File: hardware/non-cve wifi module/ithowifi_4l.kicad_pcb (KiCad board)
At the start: 4 copper layers, 63.1 x 49.8 mm, 47 parts, among them J1 USB_B_Micro, J2 RJ45_LED_Shielded, J3 Conn_Coaxial, J4 Conn_02x02_Odd_Even, J5 Conn_02x02_Odd_Even, J6 Conn_01x02_Male, Q1 BSS138, Q2 BSS138, Q3 BC847, Q4 BC847, SW1 Fail safe, U1 ESP32-WROOM, U2 CC1101-868MHz-Module, U3 CH340G, U4 AMS1117-3.3, Y1 Crystal_GND24_Small

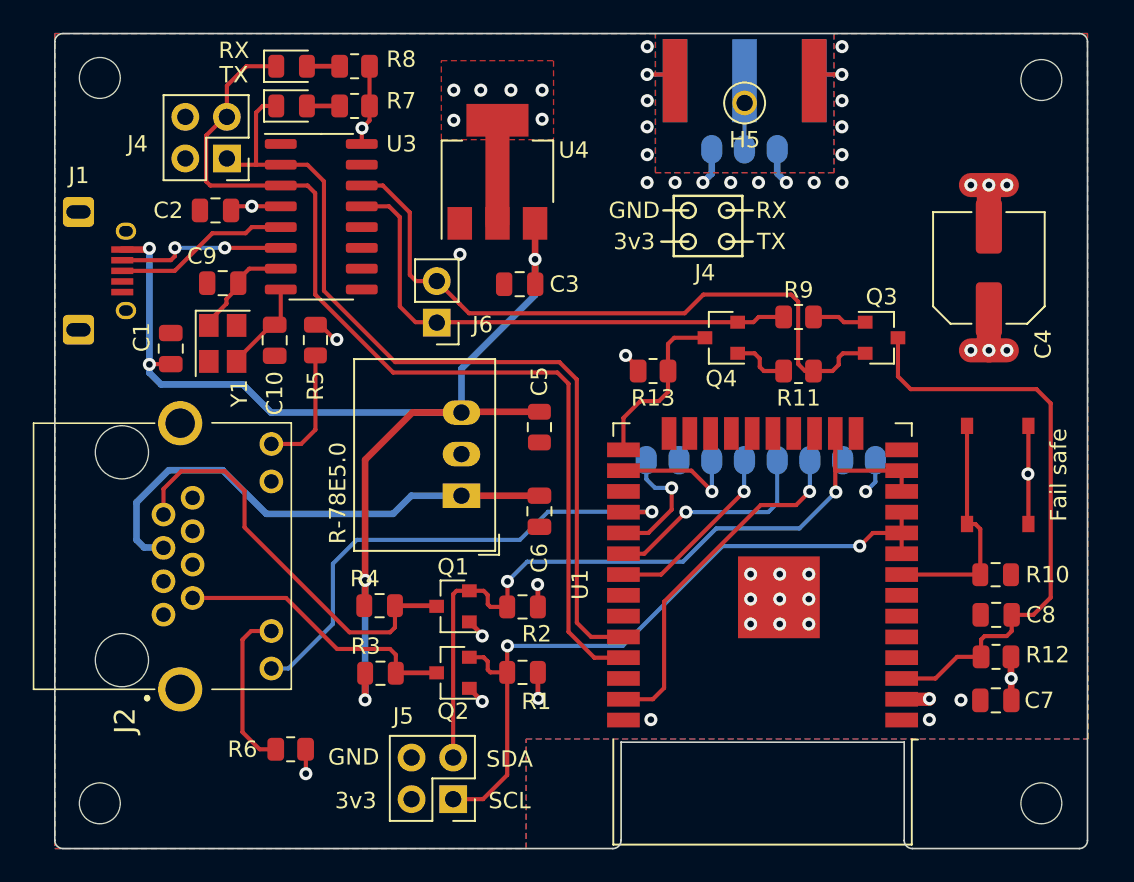
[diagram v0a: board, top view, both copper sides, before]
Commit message: Version 2.3-beta5
- fix: prevent crashes unsupported or partly supported itho devices
- breaking: On the up-side; all settings and labels have been regenerated and checked (and some translated) with a script, units have been added where available and labels are more descriptive. On the flip-side; automations based on the API, specifically the itho status label based automations might need to be updated.
- add: support for itho HeatPumt (WPU) devices and AutoTemp devices.

Please check labels for status and settings, if you see anything wrong, please let me know.
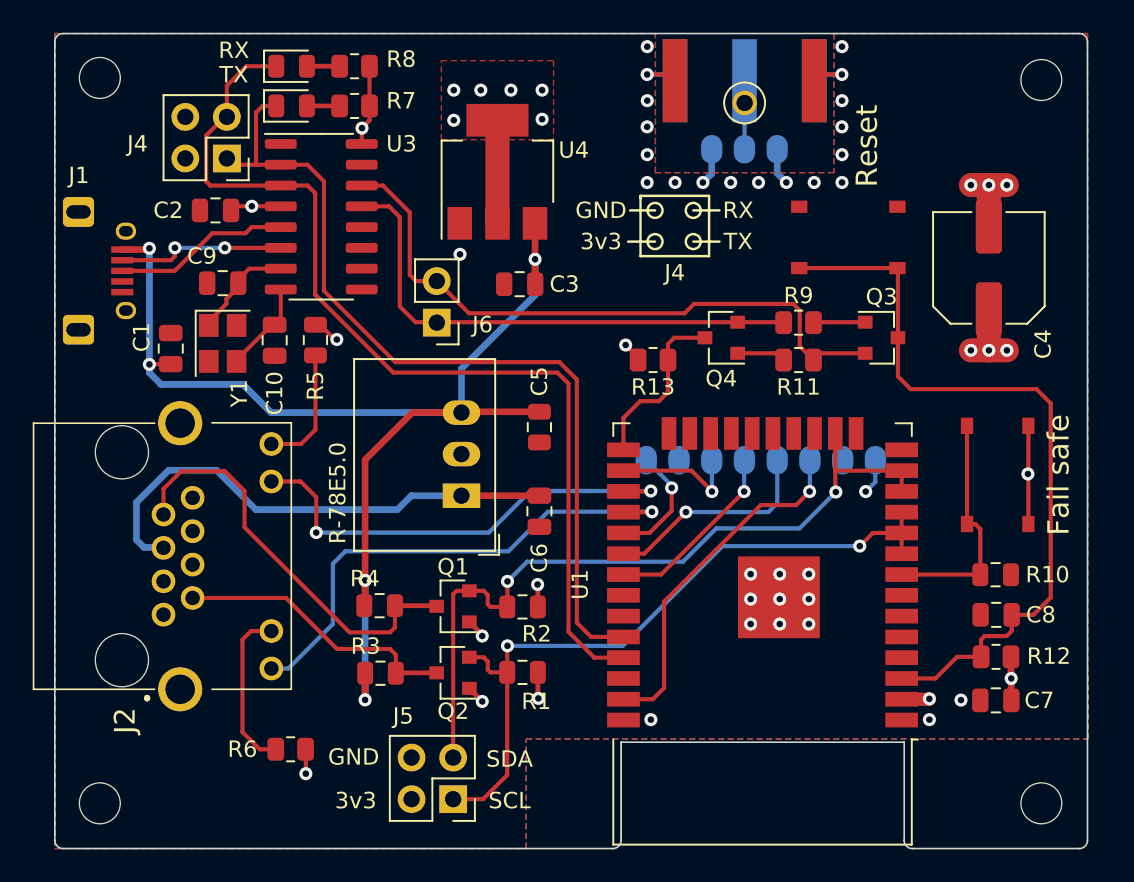
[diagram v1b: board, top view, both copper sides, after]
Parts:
- added Reset: Reset, nrg_watch:TS-1187, F.Cu at (101.2, 119.1)
- moved R11 0.67 mm to (98.2, 126.6)
- moved R13 0.67 mm to (89.3, 126.6)
- moved R9 0.35 mm to (98.2, 124.3)
- turned R12 to 0 degrees
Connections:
- J2 pad 11: GND -> D16_SYS_STATUS
- R12 pad 1: +3V3 -> EN
- R12 pad 2: EN -> +3V3
- U1 pad 27: Net-(U1-Pad27) -> D16_SYS_STATUS
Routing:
- net D16_SYS_STATUS: track 0.00 -> 32.3 mm, vias 0 -> 2
- net EN: track 36.6 -> 46.9 mm
- net RTS: track 41.6 -> 39.3 mm
- net Net-(Q4-Pad1): track 3.56 -> 2.98 mm
- net D5_SS: track 7.81 -> 7.25 mm
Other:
- board text added: "Itho HRU ESP WiFi Controller v1.2 Arjen Hiemstra - GNU GPL 3.0"
- board text removed: "Itho HRU ESP WiFi Controller v1.1 Arjen Hiemstra - GNU GPL 3.0"

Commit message: Version 2.3.5
Version 2.3.5

- fix: typo in WebAPI causing timer always being set to speed amount of minutes
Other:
- board text added: "Itho HRU ESP WiFi Controller v1.3 Arjen Hiemstra - GNU GPL 3.0"
- board text added: "https://github.com/arjenhiemstra/ithowifi"
- board text removed: "Itho HRU ESP WiFi Controller v1.2 Arjen Hiemstra - GNU GPL 3.0"
- board text removed: "https://github.com/arjenhiemstra/ithohruwifi"

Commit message: Update HW files and correct spelling
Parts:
- removed J6: Conn_01x02_Male, Connector_PinHeader_2.54mm:PinHeader_1x02_P2.54mm_Vertical
- moved C4 18.8 mm to (91.0, 120.8), turned to 0 degrees
- moved R13 11.2 mm to (100.5, 127.1), turned to 90 degrees
- moved Q4 10.6 mm to (103.9, 127.3), turned to 270 degrees
- moved SW2 9.83 mm to (110.4, 122.7), turned to 270 degrees
- moved R11 7.84 mm to (105.3, 123.3), turned to 270 degrees
- moved Q3 5.89 mm to (103.8, 119.4), turned to 90 degrees
- moved R9 4.93 mm to (103.0, 123.3), turned to 90 degrees
- renumbered Reset to SW2
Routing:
- net EN: track 46.9 -> 24.2 mm
- net DTR: track 31.9 -> 9.42 mm
- net RTS: track 39.3 -> 26.1 mm
- net +5V: track 75.6 -> 63.3 mm, vias 5 -> 4
- net D0: track 10.7 -> 0.00 mm
- net Net-(Q3-Pad1): track 3.17 -> 0.00 mm
- net Net-(Q4-Pad1): track 2.98 -> 0.00 mm
- net GND: track 16.7 -> 16.3 mm, vias 34 -> 33

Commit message: Update hardware design files
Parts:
- removed J3: Conn_Coaxial, Connector_Coaxial:SMA_Amphenol_132289_EdgeMount
- Q1, Q2, Q3, Q4: footprint Package_TO_SOT_SMD:SOT-23 -> Package_TO_SOT_SMD:SOT-23W
- U1: footprint RF_Module:ESP32-WROOM-32 -> nrg_watch:ESP32-WROOM-32E
- moved C4 11.3 mm to (79.9, 122.6)
- moved R13 11.2 mm to (89.3, 127.9), turned to 180 degrees
- moved Q4 10.5 mm to (93.5, 126.5), turned to 180 degrees
- moved R11 8.43 mm to (98.2, 127.9), turned to 180 degrees
- moved Q3 7.12 mm to (103.2, 126.5), turned to 0 degrees
- moved C3 6.39 mm to (83.7, 116.1), turned to -90 degrees
- moved H5 5.89 mm to (89.1, 110.0)
- moved R9 5.32 mm to (98.2, 125.6), turned to 0 degrees
- moved U2 3.84 mm to (94.6, 126.8)
- moved C5 2.48 mm to (80.6, 132.5)
- moved C6 2.44 mm to (80.7, 137.6)
- moved U1 2.37 mm to (98.0, 141.6)
- moved U4 2.09 mm to (78.5, 113.4)
- moved R6 2.03 mm to (65.2, 151.0)
- moved R-78E5.0 2.00 mm to (76.7, 136.7)
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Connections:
- net D0/RX0 renamed D0/RX0
- net D1/TX0 renamed D1/TX0
- J1 pad 4: Net-(J1-Pad4) -> unconnected-(J1-Pad4)
- J2 pad 1: Net-(J2-Pad1) -> unconnected-(J2-Pad1)
- J2 pad 6: Net-(J2-Pad6) -> unconnected-(J2-Pad6)
- J2 pad 8: Net-(J2-Pad8) -> unconnected-(J2-Pad8)
- U1 pad 14: Net-(U1-Pad14) -> unconnected-(U1-Pad14)
- U1 pad 17: Net-(U1-Pad17) -> unconnected-(U1-Pad17)
- U1 pad 18: Net-(U1-Pad18) -> unconnected-(U1-Pad18)
- U1 pad 19: Net-(U1-Pad19) -> unconnected-(U1-Pad19)
- U1 pad 20: Net-(U1-Pad20) -> unconnected-(U1-Pad20)
- U1 pad 21: Net-(U1-Pad21) -> unconnected-(U1-Pad21)
- U1 pad 22: Net-(U1-Pad22) -> unconnected-(U1-Pad22)
- U1 pad 23: Net-(U1-Pad23) -> unconnected-(U1-Pad23)
- U1 pad 24: Net-(U1-Pad24) -> unconnected-(U1-Pad24)
- U1 pad 32: Net-(U1-Pad32) -> unconnected-(U1-Pad32)
- U1 pad 33: Net-(U1-Pad33) -> unconnected-(U1-Pad33)
- U1 pad 36: Net-(U1-Pad36) -> unconnected-(U1-Pad36)
- U1 pad 4: Net-(U1-Pad4) -> unconnected-(U1-Pad4)
- U1 pad 5: Net-(U1-Pad5) -> unconnected-(U1-Pad5)
- U1 pad 6: Net-(U1-Pad6) -> unconnected-(U1-Pad6)
- U1 pad 7: Net-(U1-Pad7) -> unconnected-(U1-Pad7)
- U2 pad 7: Net-(U2-Pad7) -> unconnected-(U2-Pad7)
- U3 pad 10: Net-(U3-Pad10) -> unconnected-(U3-Pad10)
- U3 pad 11: Net-(U3-Pad11) -> unconnected-(U3-Pad11)
- U3 pad 12: Net-(U3-Pad12) -> unconnected-(U3-Pad12)
- U3 pad 15: Net-(U3-Pad15) -> unconnected-(U3-Pad15)
- U3 pad 9: Net-(U3-Pad9) -> unconnected-(U3-Pad9)
- Y1 pad 2: Net-(Y1-Pad2) -> unconnected-(Y1-Pad2)
- Y1 pad 4: Net-(Y1-Pad4) -> unconnected-(Y1-Pad4)
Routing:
- net DTR: track 9.42 -> 30.2 mm, vias 0 -> 2
- net +5V: track 63.3 -> 77.8 mm
- net EN: track 24.2 -> 37.5 mm
- net RTS: track 26.1 -> 38.2 mm, vias 0 -> 2
- net GND: track 16.3 -> 4.73 mm, vias 33 -> 50
- net SDA_L: track 46.9 -> 56.8 mm
- net D0: track 0.00 -> 7.68 mm
- net D23_MOSI: track 21.6 -> 15.0 mm
- net SCL_L: track 44.3 -> 50.7 mm
- net D18_SCK: track 13.3 -> 7.71 mm
- net Net-(H5-Pad1): track 4.19 -> 8.86 mm
- net D5_SS: track 7.25 -> 4.19 mm
- net Net-(Q3-Pad1): track 0.00 -> 2.97 mm
- net Net-(R10-Pad2): track 14.5 -> 11.7 mm
- net Net-(Q4-Pad1): track 0.00 -> 2.78 mm
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- added copper zone on In1.Cu, net +3V3
- added copper zone on In2.Cu, net GND
- removed copper zone on 3V3, net +3V3
- removed copper zone on GND, net GND
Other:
- outline, holes or cut-outs redrawn
- net class Default removed
- board text added: "HW rev.: 1 Batch: 04-xx22"
- board text added: "Itho NON-CVE WiFi Controller Arjen Hiemstra - GNU GPL 3.0"
- board text added: "NL5"
- board text removed: "Itho HRU ESP WiFi Controller v1.3 Arjen Hiemstra - GNU GPL 3.0"

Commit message: update hardware files
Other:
- board text added: "HW rev.: 1 Batch: 04-1222"
- board text added: "Itho NON-CVE WiFi Controller Arjen Hiemstra - GNU GPL 3.0 https://github.com/arjenhiemstra/ithowifi"
- board text removed: "HW rev.: 1 Batch: 04-xx22"
- board text removed: "Itho NON-CVE WiFi Controller Arjen Hiemstra - GNU GPL 3.0"
- board text removed: "https://github.com/arjenhiemstra/ithowifi"

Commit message: Update hardware files
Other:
- board text added: "HW rev.: 1 Batch: 05-1722"
- board text removed: "HW rev.: 1 Batch: 04-1222"
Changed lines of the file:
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@@
       (drillshape 0)
       (scaleselection 1)
-      (outputdirectory "gerbers 1.4 4layer/")
+      (outputdirectory "gerbers 1.5 4layer/")
     )
   )
@@
     (effects (font (size 1.246 1.246) (thickness 0.2)) (justify right mirror))
   )
-  (gr_text "HW rev.: 1\nBatch: 04-1222\n" (at 68.199 109.601 270) (layer "B.SilkS")
+  (gr_text "HW rev.: 1\nBatch: 05-1722\n" (at 68.199 109.601 270) (layer "B.SilkS")
     (effects (font (size 1.246 1.246) (thickness 0.2)) (justify right mirror))
   )
@@
     (pts (xy 89.0524 110.3884) (xy 93.1418 110.3503))
     (height -11.090003)
-    (gr_text "161.0070 mils" (at 90.977012 97.479906 0.5337961658) (layer "Dwgs.User")
+    (gr_text "4.0896 mm" (at 90.977012 97.479906 0.5337961658) (layer "Dwgs.User")
       (effects (font (size 1.5 1.5) (thickness 0.3)))
     )
@@
     (pts (xy 88.646 113.03) (xy 88.646 110.0201))
     (height 15.5194)
-    (gr_text "118.5000 mils" (at 102.3654 111.52505 90) (layer "Dwgs.User")
+    (gr_text "3.0099 mm" (at 102.3654 111.52505 90) (layer "Dwgs.User")
       (effects (font (size 1.5 1.5) (thickness 0.3)))
     )
@@
     (pts (xy 88.646 110.0328) (xy 88.646 107.0229))
     (height 15.5194)
-    (gr_text "118.5000 mils" (at 102.3654 108.52785 90) (layer "Dwgs.User")
+    (gr_text "3.0099 mm" (at 102.3654 108.52785 90) (layer "Dwgs.User")
       (effects (font (size 1.5 1.5) (thickness 0.3)))
     )
@@
     (pts (xy 89.0524 110.3884) (xy 109.0676 110.4011))
     (height -6.832613)
-    (gr_text "788.0002 mils" (at 99.065477 101.762138 359.9636448) (layer "Dwgs.User")
+    (gr_text "20.0152 mm" (at 99.065477 101.762138 359.9636448) (layer "Dwgs.User")
       (effects (font (size 1.5 1.5) (thickness 0.3)))
     )

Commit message: Update hardware files
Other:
- board text added: "HW rev.: 1 Batch: 06-3422"
- board text removed: "HW rev.: 1 Batch: 05-1722"
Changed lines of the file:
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@@
       (drillshape 0)
       (scaleselection 1)
-      (outputdirectory "gerbers 1.5 4layer/")
+      (outputdirectory "gerbers 1.6 4layer/")
     )
   )
@@
     (effects (font (size 1.246 1.246) (thickness 0.2)) (justify right mirror))
   )
-  (gr_text "HW rev.: 1\nBatch: 05-1722\n" (at 68.199 109.601 270) (layer "B.SilkS")
+  (gr_text "HW rev.: 1\nBatch: 06-3422\n" (at 68.199 109.601 270) (layer "B.SilkS")
     (effects (font (size 1.246 1.246) (thickness 0.2)) (justify right mirror))
   )

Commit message: Update hardware files
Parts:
- U5: renamed from R-78E5.0; value U2 -> R-78E5.0
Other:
- board text added: "HW rev.: 1 Batch: 09-4922"
- board text removed: "HW rev.: 1 Batch: 06-3422"
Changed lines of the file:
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@@
       (drillshape 0)
       (scaleselection 1)
-      (outputdirectory "gerbers 1.6 4layer/")
+      (outputdirectory "gerbers 1.9 4layer/")
     )
   )
@@
     (property "Sheetname" "")
     (attr through_hole)
-    (fp_text reference "R-78E5.0" (at 9.178 -1.3439 180) (layer "F.SilkS")
-      (effects (font (size 1 1) (thickness 0.15)))
-    )
-    (fp_text value "U2" (at 2.54 3 90) (layer "F.Fab")
+    (fp_text reference "U5" (at 9.178 -1.3439 180) (layer "F.SilkS")
+      (effects (font (size 1 1) (thickness 0.15)))
+    )
+    (fp_text value "R-78E5.0" (at 2.54 3 90) (layer "F.Fab")
       (effects (font (size 1 1) (thickness 0.15)))
     )
@@
       (effects (font (size 1.27 1.27) (thickness 0.254)))
     )
+    (fp_line (start 4.56 7.94) (end 4.56 0.54) (layer "F.SilkS") (width 0.1))
+    (fp_line (start 5.2 1) (end 5.2 1) (layer "F.SilkS") (width 0.2))
+    (fp_line (start 5 1) (end 5 1) (layer "F.SilkS") (width 0.2))
+    (fp_line (start -11.72 -7.81) (end 4.56 -7.81) (layer "F.SilkS") (width 0.1))
+    (fp_line (start -11.72 -2.96) (end -11.72 -7.81) (layer "F.SilkS") (width 0.1))
     (fp_line (start -11.7 7.94) (end 4.56 7.94) (layer "F.SilkS") (width 0.1))
-    (fp_line (start -11.72 -2.96) (end -11.72 -7.81) (layer "F.SilkS") (width 0.1))
     (fp_line (start 4.56 -7.81) (end 4.56 -2.96) (layer "F.SilkS") (width 0.1))
-    (fp_line (start 5 1) (end 5 1) (layer "F.SilkS") (width 0.2))
-    (fp_line (start 5.2 1) (end 5.2 1) (layer "F.SilkS") (width 0.2))
-    (fp_line (start -11.72 -7.81) (end 4.56 -7.81) (layer "F.SilkS") (width 0.1))
-    (fp_line (start 4.56 7.94) (end 4.56 0.54) (layer "F.SilkS") (width 0.1))
     (fp_line (start -11.7 0.54) (end -11.7 7.94) (layer "F.SilkS") (width 0.1))
     (fp_arc (start 5.2 1) (mid 5.1 1.1) (end 5 1) (layer "F.SilkS") (width 0.2))
     (fp_arc (start 5 1) (mid 5.1 0.9) (end 5.2 1) (layer "F.SilkS") (width 0.2))
-    (fp_line (start 6.91 8.94) (end -14.05 8.94) (layer "F.CrtYd") (width 0.1))
-    (fp_line (start -14.05 -8.81) (end 6.91 -8.81) (layer "F.CrtYd") (width 0.1))
     (fp_line (start -14.05 8.94) (end -14.05 -8.81) (layer "F.CrtYd") (width 0.1))
     (fp_line (start 6.91 -8.81) (end 6.91 8.94) (layer "F.CrtYd") (width 0.1))
+    (fp_line (start -14.05 -8.81) (end 6.91 -8.81) (layer "F.CrtYd") (width 0.1))
+    (fp_line (start 6.91 8.94) (end -14.05 8.94) (layer "F.CrtYd") (width 0.1))
+    (fp_line (start -11.7 7.94) (end -11.7 -7.81) (layer "F.Fab") (width 0.2))
     (fp_line (start -11.7 -7.81) (end 4.56 -7.81) (layer "F.Fab") (width 0.2))
     (fp_line (start 4.56 7.94) (end -11.7 7.94) (layer "F.Fab") (width 0.2))
-    (fp_line (start -11.7 7.94) (end -11.7 -7.81) (layer "F.Fab") (width 0.2))
     (fp_line (start 4.56 -7.81) (end 4.56 7.94) (layer "F.Fab") (width 0.2))
-    (pad "" np_thru_hole circle locked (at 2.78 2.54 270) (size 3.25 0) (drill 3.25) (layers *.Cu *.Mask))
-    (pad "" np_thru_hole circle locked (at -9.92 2.54 270) (size 3.25 0) (drill 3.25) (layers *.Cu *.Mask))
-    (pad "1" thru_hole circle locked (at 0 0 270) (size 1.446 1.446) (drill 0.89) (layers *.Cu *.Mask)
+    (pad "" np_thru_hole circle (at 2.78 2.54 270) (size 3.25 3.25) (drill 3.25) (layers F&B.Cu *.Mask))
+    (pad "" np_thru_hole circle (at -9.92 2.54 270) (size 3.25 3.25) (drill 3.25) (layers F&B.Cu *.Mask))
+    (pad "1" thru_hole circle (at 0 0 270) (size 1.446 1.446) (drill 0.89) (layers *.Cu *.Mask)
       (net 11 "unconnected-(J2-Pad1)") (pintype "passive+no_connect"))
-    (pad "2" thru_hole circle locked (at -1.02 -1.78 270) (size 1.446 1.446) (drill 0.89) (layers *.Cu *.Mask)
+    (pad "2" thru_hole circle (at -1.02 -1.78 270) (size 1.446 1.446) (drill 0.89) (layers *.Cu *.Mask)
       (net 39 "Net-(J2-Pad2)") (pintype "passive"))
-    (pad "3" thru_hole circle locked (at -2.04 0 270) (size 1.446 1.446) (drill 0.89) (layers *.Cu *.Mask)
+    (pad "3" thru_hole circle (at -2.04 0 270) (size 1.446 1.446) (drill 0.89) (layers *.Cu *.Mask)
       (net 1 "GND") (pintype "passive"))
-    (pad "4" thru_hole circle locked (at -3.06 -1.78 270) (size 1.446 1.446) (drill 0.89) (layers *.Cu *.Mask)
+    (pad "4" thru_hole circle (at -3.06 -1.78 270) (size 1.446 1.446) (drill 0.89) (layers *.Cu *.Mask)
       (net 1 "GND") (pintype "passive"))
-    (pad "5" thru_hole circle locked (at -4.08 0 270) (size 1.446 1.446) (drill 0.89) (layers *.Cu *.Mask)
+    (pad "5" thru_hole circle (at -4.08 0 270) (size 1.446 1.446) (drill 0.89) (layers *.Cu *.Mask)
       (net 18 "+15V") (pintype "passive"))
-    (pad "6" thru_hole circle locked (at -5.1 -1.78 270) (size 1.446 1.446) (drill 0.89) (layers *.Cu *.Mask)
+    (pad "6" thru_hole circle (at -5.1 -1.78 270) (size 1.446 1.446) (drill 0.89) (layers *.Cu *.Mask)
       (net 19 "unconnected-(J2-Pad6)") (pintype "passive+no_connect"))
-    (pad "7" thru_hole circle locked (at -6.12 0 270) (size 1.446 1.446) (drill 0.89) (layers *.Cu *.Mask)
+    (pad "7" thru_hole circle (at -6.12 0 270) (size 1.446 1.446) (drill 0.89) (layers *.Cu *.Mask)
       (net 40 "Net-(J2-Pad7)") (pintype "passive"))
-    (pad "8" thru_hole circle locked (at -7.14 -1.78 270) (size 1.446 1.446) (drill 0.89) (layers *.Cu *.Mask)
+    (pad "8" thru_hole circle (at -7.14 -1.78 270) (size 1.446 1.446) (drill 0.89) (layers *.Cu *.Mask)
       (net 20 "unconnected-(J2-Pad8)") (pintype "passive+no_connect"))
-    (pad "9" thru_hole circle locked (at 3.29 -6.59 270) (size 1.446 1.446) (drill 0.89) (layers *.Cu *.Mask)
+    (pad "9" thru_hole circle (at 3.29 -6.59 270) (size 1.446 1.446) (drill 0.89) (layers *.Cu *.Mask)
       (net 21 "D17_WIFI_STATUS") (pintype "passive"))
-    (pad "10" thru_hole circle locked (at 1 -6.59 270) (size 1.446 1.446) (drill 0.89) (layers *.Cu *.Mask)
+    (pad "10" thru_hole circle (at 1 -6.59 270) (size 1.446 1.446) (drill 0.89) (layers *.Cu *.Mask)
       (net 32 "Net-(J2-Pad10)") (pintype "passive"))
-    (pad "11" thru_hole circle locked (at -8.14 -6.59 270) (size 1.446 1.446) (drill 0.89) (layers *.Cu *.Mask)
+    (pad "11" thru_hole circle (at -8.14 -6.59 270) (size 1.446 1.446) (drill 0.89) (layers *.Cu *.Mask)
       (net 43 "D16_SYS_STATUS") (pintype "passive"))
-    (pad "12" thru_hole circle locked (at -10.43 -6.59 270) (size 1.446 1.446) (drill 0.89) (layers *.Cu *.Mask)
+    (pad "12" thru_hole circle (at -10.43 -6.59 270) (size 1.446 1.446) (drill 0.89) (layers *.Cu *.Mask)
       (net 33 "Net-(J2-Pad12)") (pintype "passive"))
-    (pad "MH1" thru_hole circle locked (at -11.7 -1.02 270) (size 2.7 2.7) (drill 1.8) (layers *.Cu *.Mask))
-    (pad "MH2" thru_hole circle locked (at 4.56 -1.02 270) (size 2.7 2.7) (drill 1.8) (layers *.Cu *.Mask))
+    (pad "MH1" thru_hole circle (at -11.7 -1.02 270) (size 2.7 2.7) (drill 1.8) (layers *.Cu *.Mask))
+    (pad "MH2" thru_hole circle (at 4.56 -1.02 270) (size 2.7 2.7) (drill 1.8) (layers *.Cu *.Mask))
     (model "R-RJ45R08P-C000.stp"
-      (offset (xyz 0 0 0))
+      (offset (xyz -0.0000000000000004 -0.0000000000000002 0))
       (scale (xyz 1 1 1))
       (rotate (xyz 0 0 0))
@@
     (effects (font (size 1.246 1.246) (thickness 0.2)) (justify right mirror))
   )
-  (gr_text "HW rev.: 1\nBatch: 06-3422\n" (at 68.199 109.601 270) (layer "B.SilkS")
+  (gr_text "HW rev.: 1\nBatch: 09-4922\n" (at 68.199 109.601 270) (layer "B.SilkS")
     (effects (font (size 1.246 1.246) (thickness 0.2)) (justify right mirror))
   )
